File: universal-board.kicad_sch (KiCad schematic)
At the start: 44 parts, among them J1 USB_C_Receptacle, J2 Conn_02x04_Odd_Even, J3 Conn_01x08, J4 CONN_WS2812, J5 CONN_I2C_GROVE, J6 CONN_UART, Q1 BSS138, SW1 SW_RESET, SW2 SW_ACK, U2 AMS1117-3.3, U4 USBLC6-2SC6, U5 74AHCT1G125, U6 TSOP384xx, U7 ESP32-S3-WROOM-1-N16

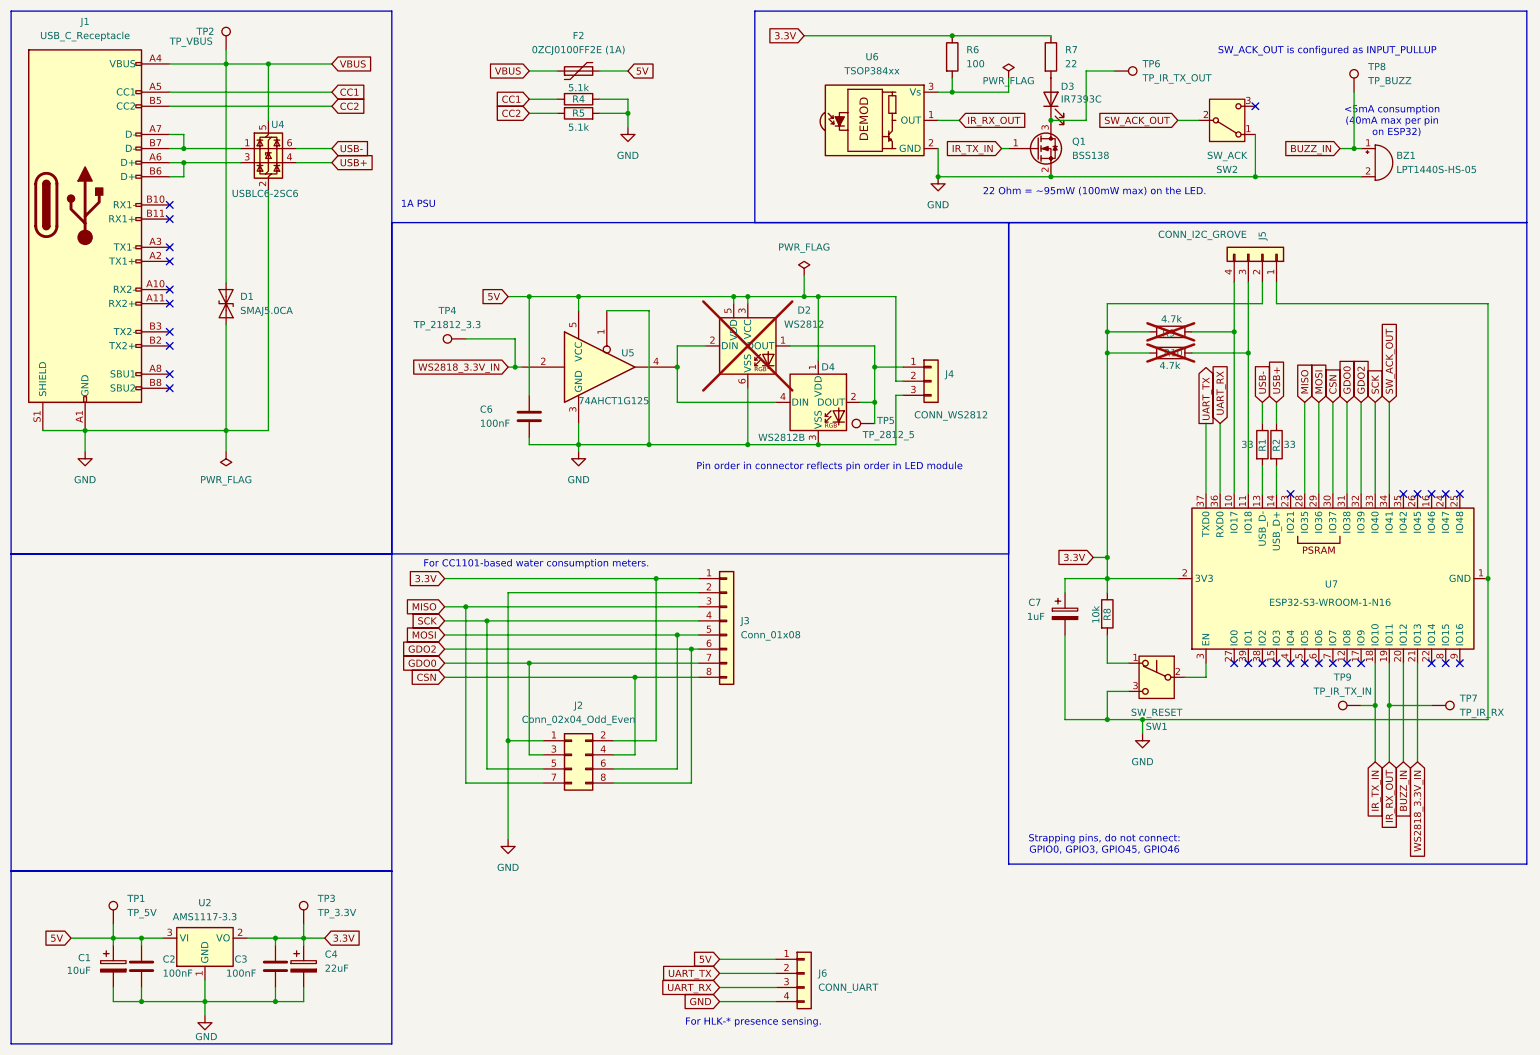
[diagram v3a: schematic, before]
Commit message: Added TVS diodes to USB and resistors.
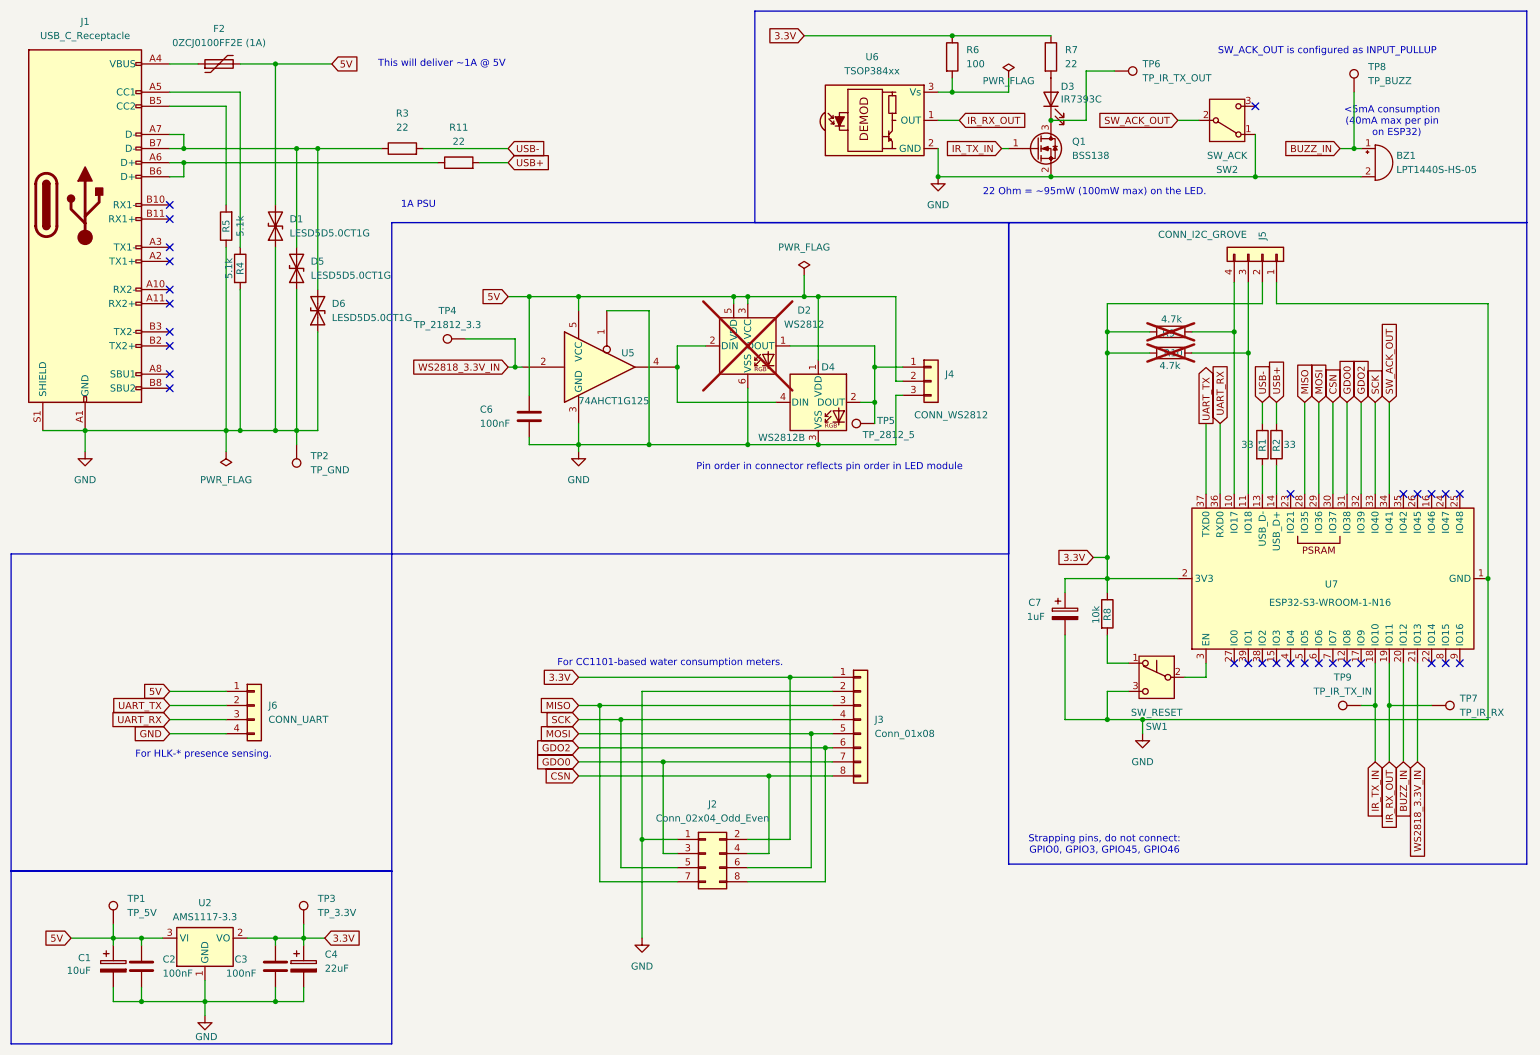
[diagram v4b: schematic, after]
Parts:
- removed D1: SMAJ5.0CA, Diode_SMD:D_SMA, symbol Diode:SMAJ5.0CA
- removed U4: USBLC6-2SC6, Package_TO_SOT_SMD:SOT-23-6, symbol Power_Protection:USBLC6-2SC6
- added D1, D5, D6: LESD5D5.0CT1G, symbol Device:D_TVS
- added R11, R3: 22, symbol Device:R
- TP2: value TP_VBUS -> TP_GND; footprint TestPoint:TestPoint_Pad_D2.0mm -> (none)
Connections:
- net 5V: now also D1.2 (A2)
- net GND: now also R4.2, R5.1, TP2.1, D1.1 (A1), D5.1 (A1), D6.1 (A1); no longer R4.1, R5.2
- net USB+: now also R11.2
- net USB-: now also R3.2
- net at J1.A7 (D-), J1.B7 (D-): now also D5.2 (A2), D6.2 (A2), R3.1
- net at J1.A6 (D+), J1.B6 (D+): now also R11.1
- net CC1: no longer names the net of J1.A5 (CC1)
- net CC1: now also R4.1; no longer R4.2
- net CC2: no longer names the net of J1.B5 (CC2)
- net CC2: now also R5.2; no longer R5.1
- net VBUS: no longer names the net of F2.1, J1.A4 (VBUS), J1.A9 (VBUS), J1.B4 (VBUS), J1.B9 (VBUS)
- net VBUS: no longer TP2.1
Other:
- note added: "This will deliver ~1A @ 5V"
- moved on the sheet: F2, J2, J3, J6, R4, R5

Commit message: Used ESP32-S2-MINI-2 in place of the curret module.
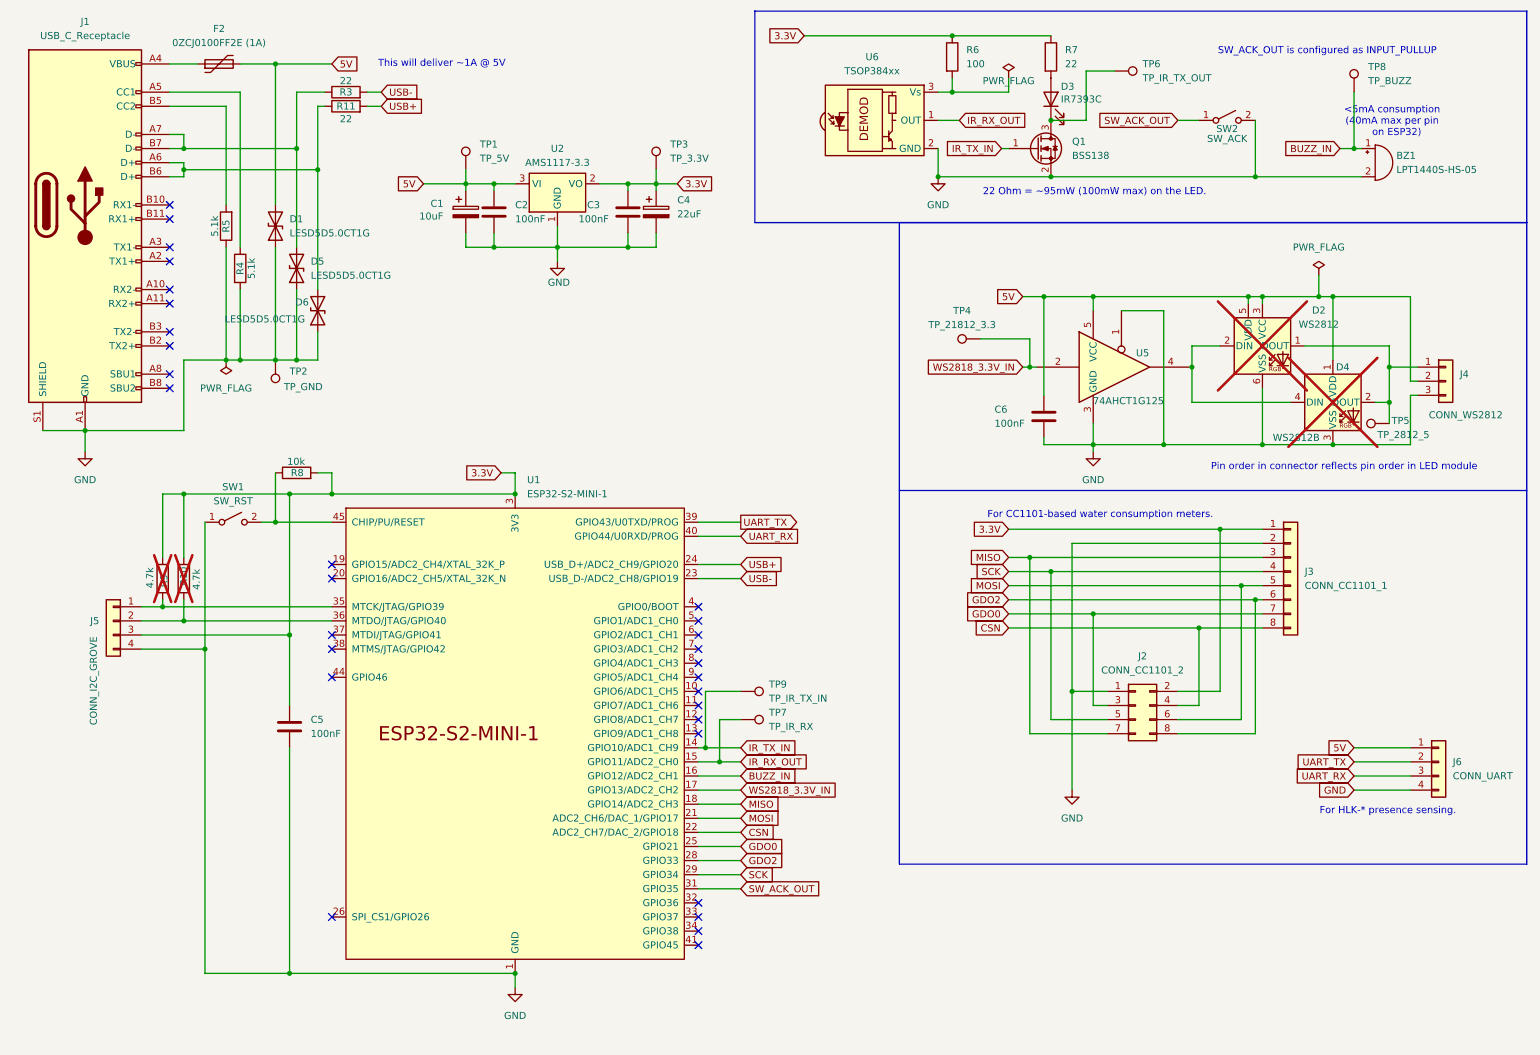
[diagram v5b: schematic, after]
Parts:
- removed C7: 1uF, Capacitor_THT:CP_Radial_D5.0mm_P2.50mm, symbol Device:C_Polarized
- removed R1, R2: 33, symbol Device:R
- removed SW1: SW_RESET, Button_Switch_THT:SW_PUSH_6mm, symbol Switch:SW_Push_SPDT
- removed SW2: SW_ACK, Button_Switch_THT:SW_PUSH_6mm, symbol Switch:SW_SPDT
- removed U7: ESP32-S3-WROOM-1-N16, RF_Module:ESP32-S3-WROOM-1, symbol RF_Module:ESP32-S3-WROOM-1
- added C5: 100nF, symbol Device:C
- added SW1: SW_RST, symbol Switch:SW_SPST
- added SW2: SW_ACK, symbol Switch:SW_SPST
- added U1: ESP32-S2-MINI-1, PCM_Espressif:ESP32-S2-MINI-1, symbol PCM_Espressif:ESP32-S2-MINI-1
- D4: now not fitted
- J2: value Conn_02x04_Odd_Even -> CONN_CC1101_2
- J3: value Conn_01x08 -> CONN_CC1101_1
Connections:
- net 3.3V: now also J5.3 (Pin_3), R10.1, R8.2, R9.2, C5.1, U1.3 (3V3); no longer J5.2 (Pin_2), R10.2, R8.1, R9.1
- net BUZZ_IN: now also U1.16 (GPIO12/ADC2_CH1)
- net CSN: now also U1.22 (ADC2_CH7/DAC_2/GPIO18)
- net GDO0: now also U1.25 (GPIO21)
- net GDO2: now also U1.28 (GPIO33)
- net GND: now also J5.4 (Pin_4), C5.2, SW1.1 (A), SW2.2 (B), U1.1 (GND), U1.2 (GND), U1.30 (GND), U1.42 (GND), U1.43 (GND), U1.46 (GND), U1.47 (GND), U1.48 (GND), U1.49 (GND), U1.50 (GND), U1.51 (GND), U1.52 (GND), U1.53 (GND), U1.54 (GND), U1.55 (GND), U1.56 (GND), U1.57 (GND), U1.58 (GND), U1.59 (GND), U1.60 (GND), U1.61 (GND), U1.62 (GND), U1.63 (GND), U1.64 (GND), U1.65 (GND); no longer J5.1 (Pin_1)
- net IR_RX_OUT: now also U1.15 (GPIO11/ADC2_CH0)
- net IR_TX_IN: now also U1.14 (GPIO10/ADC1_CH9)
- net MISO: now also U1.18 (GPIO14/ADC2_CH3)
- net MOSI: now also U1.21 (ADC2_CH6/DAC_1/GPIO17)
- net SCK: now also U1.29 (GPIO34)
- net SW_ACK_OUT: now also SW2.1 (A), U1.31 (GPIO35)
- net UART_RX: now also U1.40 (GPIO44/U0RXD/PROG)
- net UART_TX: now also U1.39 (GPIO43/U0TXD/PROG)
- net USB+: now also U1.24 (USB_D+/ADC2_CH9/GPIO20)
- net USB-: now also U1.23 (USB_D-/ADC2_CH8/GPIO19)
- net WS2818_3.3V_IN: now also U1.17 (GPIO13/ADC2_CH2)
- net at D5.2 (A2), J1.A7 (D-), J1.B7 (D-)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: no longer D6.2 (A2)
- net at J1.A6 (D+), J1.B6 (D+), R11.1: now also D6.2 (A2)
- new net: R8.1, SW1.2 (B), U1.45 (CHIP/PU/RESET)
- new net: J5.1 (Pin_1), R9.1, U1.35 (MTCK/JTAG/GPIO39)
- new net: J5.2 (Pin_2), R10.2, U1.36 (MTDO/JTAG/GPIO40)
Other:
- note removed: "1A PSU"
- note removed: "Strapping pins, do not connect: GPIO0, GPIO3, GPIO45, GPIO46"
- moved on the sheet: C1, C2, C3, C4, C6, D2, J2, J3, J4, J5, J6, R10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

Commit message: Renumbered components.
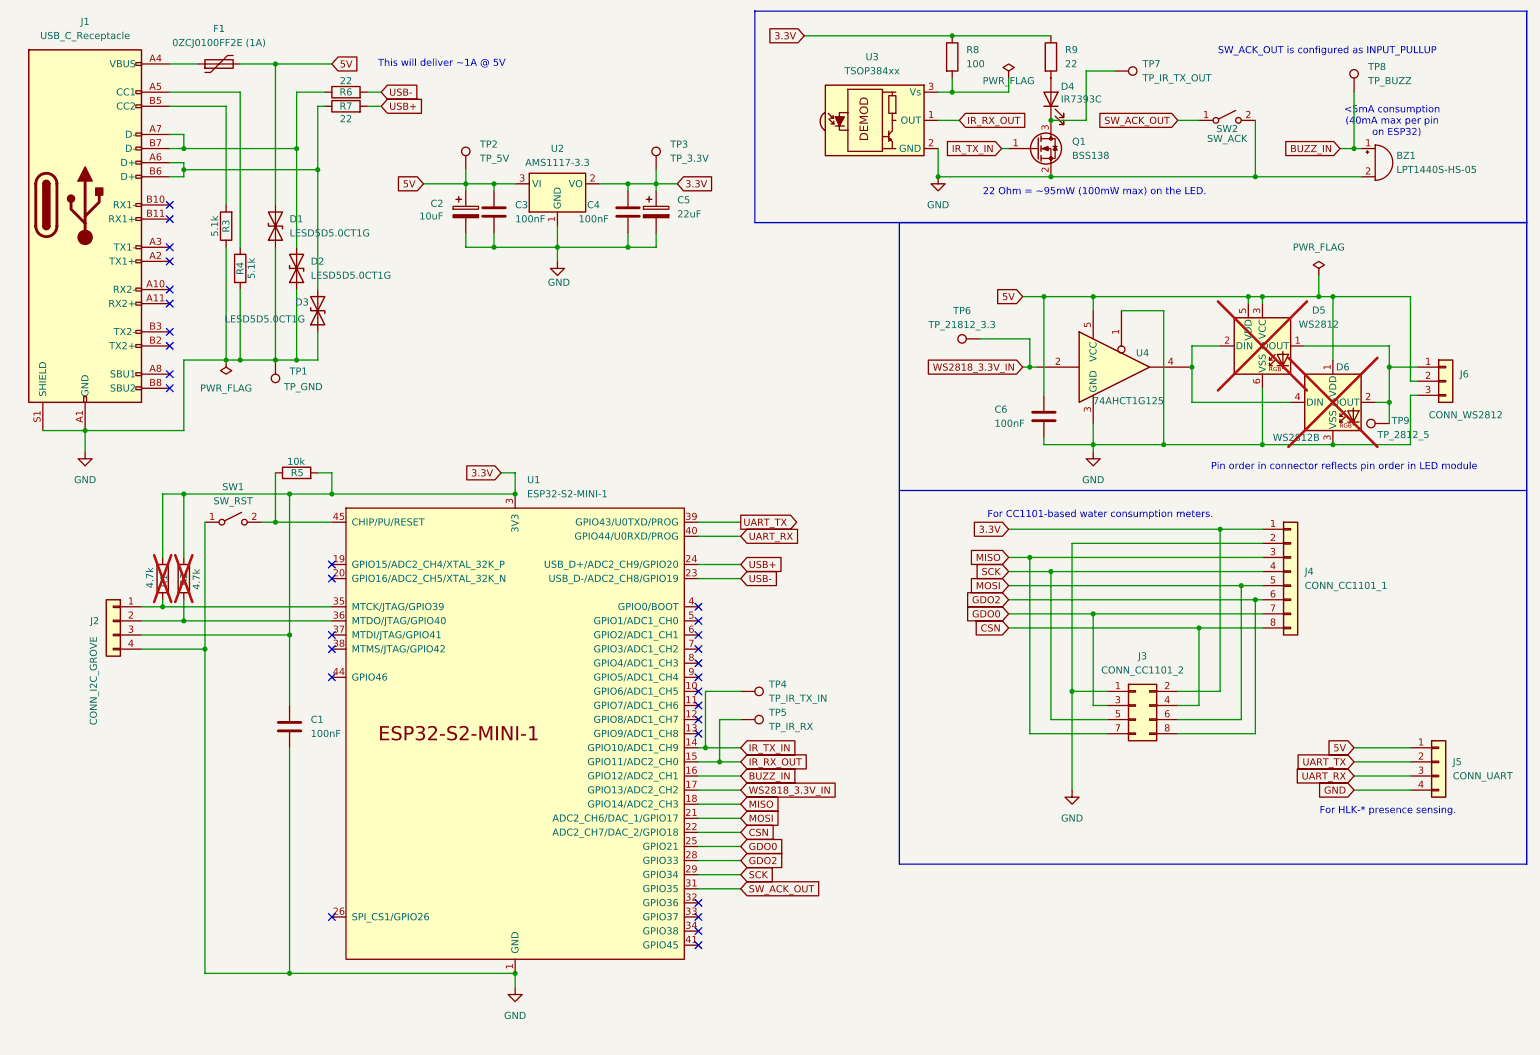
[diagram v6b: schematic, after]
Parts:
- renumbered C5 to C1, C1 to C2, C2 to C3, C3 to C4, C4 to C5, D5 to D2, D6 to D3, D3 to D4, D2 to D5, D4 to D6, F2 to F1, J5 to J2, J2 to J3, J3 to J4, J6 to J5, J4 to J6, R9 to R1, R10 to R2, R5 to R3, R8 to R5, R3 to R6, R11 to R7, R6 to R8, R7 to R9, TP2 to TP1, TP1 to TP2, TP9 to TP4, TP7 to TP5, TP4 to TP6, TP6 to TP7, TP5 to TP9, U6 to U3, U5 to U4

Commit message: Footprints assigned
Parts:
- C1: footprint (none) -> Capacitor_SMD:C_1206_3216Metric_Pad1.33x1.80mm_HandSolder
- D1, D2, D3: footprint (none) -> Diode_SMD:D_SOD-523
- R6, R7: footprint (none) -> Resistor_SMD:R_1206_3216Metric_Pad1.30x1.75mm_HandSolder
- SW1, SW2: footprint (none) -> Button_Switch_THT:SW_PUSH_6mm
- TP1: footprint (none) -> TestPoint:TestPoint_Pad_4.0x4.0mm
- U4: footprint Package_TO_SOT_SMD:SOT-353_SC-70-5_Handsoldering -> Package_TO_SOT_SMD:SOT-353_SC-70-5
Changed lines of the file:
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@@
 			)
 		)
-		(property "Footprint" ""
+		(property "Footprint" "Button_Switch_THT:SW_PUSH_6mm"
 			(at 52.07 104.14 0)
 			(effects
@@
 			)
 		)
-		(property "Footprint" ""
+		(property "Footprint" "Diode_SMD:D_SOD-523"
 			(at 67.31 66.04 0)
 			(effects
@@
 			)
 		)
-		(property "Footprint" ""
+		(property "Footprint" "Resistor_SMD:R_1206_3216Metric_Pad1.30x1.75mm_HandSolder"
 			(at 72.39 28.448 90)
 			(effects
@@
 			)
 		)
-		(property "Footprint" ""
+		(property "Footprint" "Diode_SMD:D_SOD-523"
 			(at 59.69 50.8 0)
 			(effects
@@
 			)
 		)
-		(property "Footprint" ""
+		(property "Footprint" "Diode_SMD:D_SOD-523"
 			(at 63.5 58.42 0)
 			(effects
@@
 			)
 		)
-		(property "Footprint" ""
+		(property "Footprint" "TestPoint:TestPoint_Pad_4.0x4.0mm"
 			(at 54.61 74.93 0)
 			(effects
@@
 			)
 		)
-		(property "Footprint" ""
+		(property "Footprint" "Capacitor_SMD:C_1206_3216Metric_Pad1.33x1.80mm_HandSolder"
 			(at 63.1952 144.78 0)
 			(effects
@@
 			)
 		)
-		(property "Footprint" ""
+		(property "Footprint" "Button_Switch_THT:SW_PUSH_6mm"
 			(at 231.14 31.75 0)
 			(effects
@@
 			)
 		)
-		(property "Footprint" ""
+		(property "Footprint" "Resistor_SMD:R_1206_3216Metric_Pad1.30x1.75mm_HandSolder"
 			(at 72.39 30.988 90)
 			(effects
@@
 			)
 		)
-		(property "Footprint" "Package_TO_SOT_SMD:SOT-353_SC-70-5_Handsoldering"
+		(property "Footprint" "Package_TO_SOT_SMD:SOT-353_SC-70-5"
 			(at 212.09 76.2 0)
 			(effects

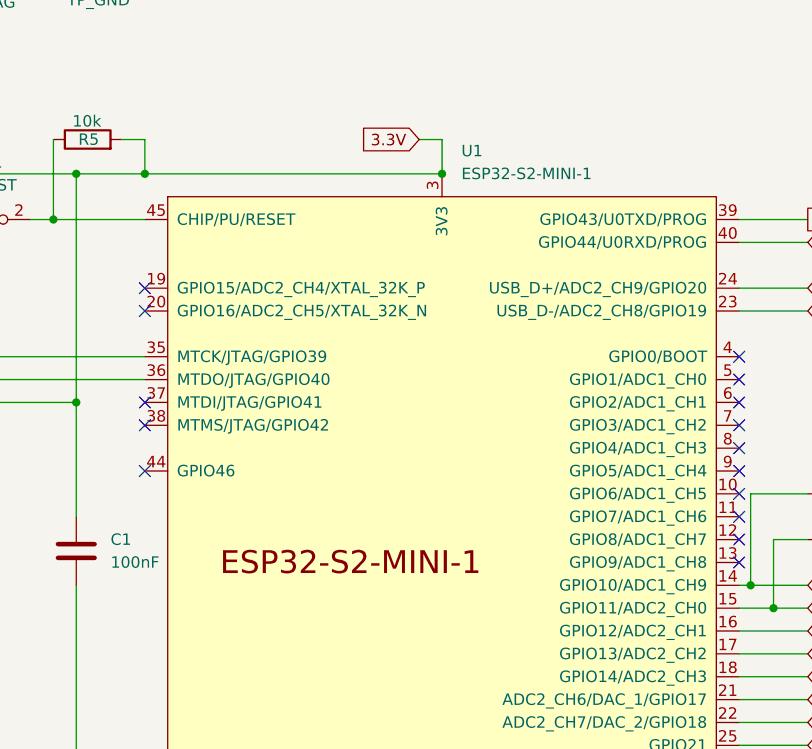
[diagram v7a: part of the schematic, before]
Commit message: Updated part number on schematic for ESP32
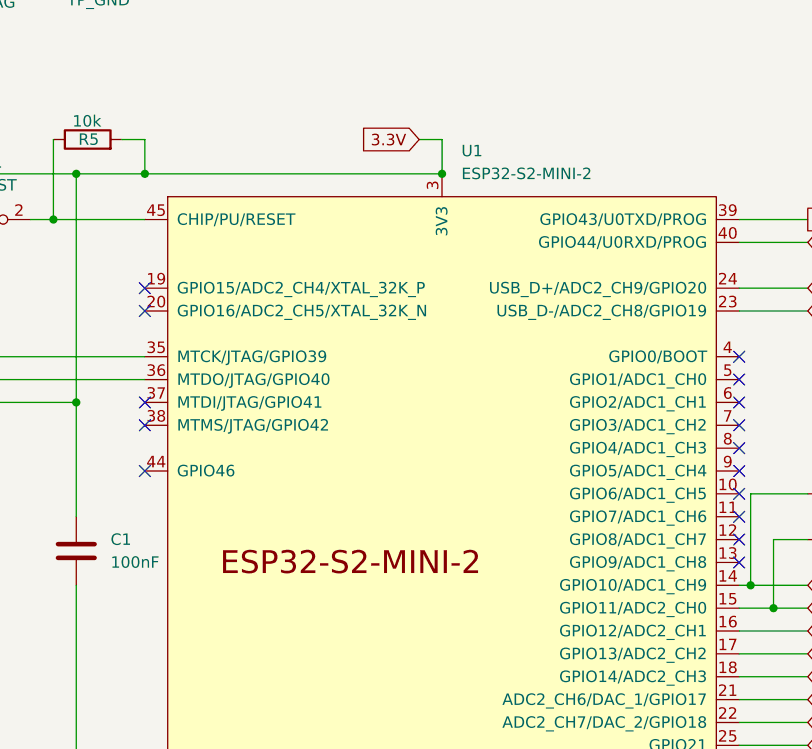
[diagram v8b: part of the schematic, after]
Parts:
- U1: value ESP32-S2-MINI-1 -> ESP32-S2-MINI-2
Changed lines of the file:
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@@
 			)
 		)
-		(property "Value" "ESP32-S2-MINI-1"
+		(property "Value" "ESP32-S2-MINI-2"
 			(at 105.0133 99.06 0)
 			(effects
